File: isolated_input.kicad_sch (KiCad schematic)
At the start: 4 parts, among them U7 EL357N-G

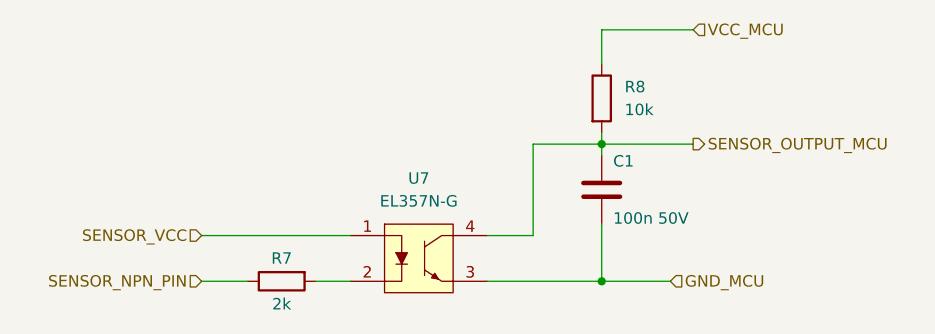
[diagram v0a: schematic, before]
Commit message: Refactored top sheet
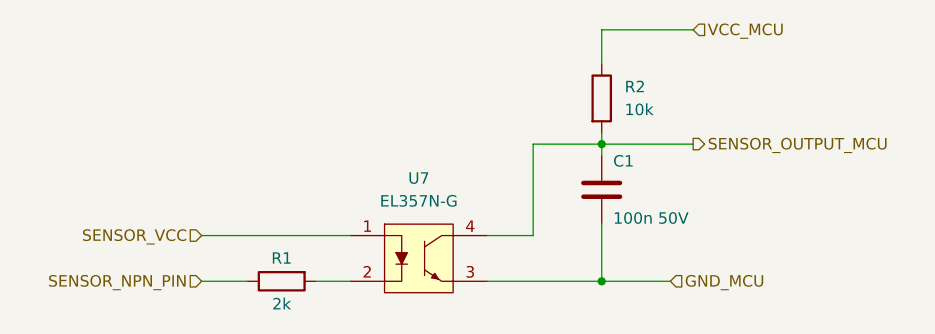
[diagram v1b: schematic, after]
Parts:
- renumbered R7 to R1, R8 to R2
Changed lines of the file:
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@@
   (symbol (lib_id "Device:R") (at 132.08 96.52 90) (mirror x) (unit 1)
     (in_bom yes) (on_board yes)
-    (property "Reference" "R7" (id 0) (at 132.08 93.98 90))
+    (property "Reference" "R1" (id 0) (at 132.08 93.98 90))
     (property "Value" "2k" (id 1) (at 132.08 99.06 90))
     (property "Footprint" "Resistor_SMD:R_1206_3216Metric" (id 2) (at 132.08 94.742 90)
@@
   (symbol (lib_id "Device:R") (at 167.64 76.2 0) (unit 1)
     (in_bom yes) (on_board yes) (fields_autoplaced)
-    (property "Reference" "R8" (id 0) (at 170.18 74.9299 0)
+    (property "Reference" "R2" (id 0) (at 170.18 74.9299 0)
       (effects (font (size 1.27 1.27)) (justify left))
     )
